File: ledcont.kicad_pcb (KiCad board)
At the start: 2 copper layers, 22 parts, among them J1 Screw_Terminal_01x02, J2 Screw_Terminal_01x02, U1 PAM2804, U2 TSM102A

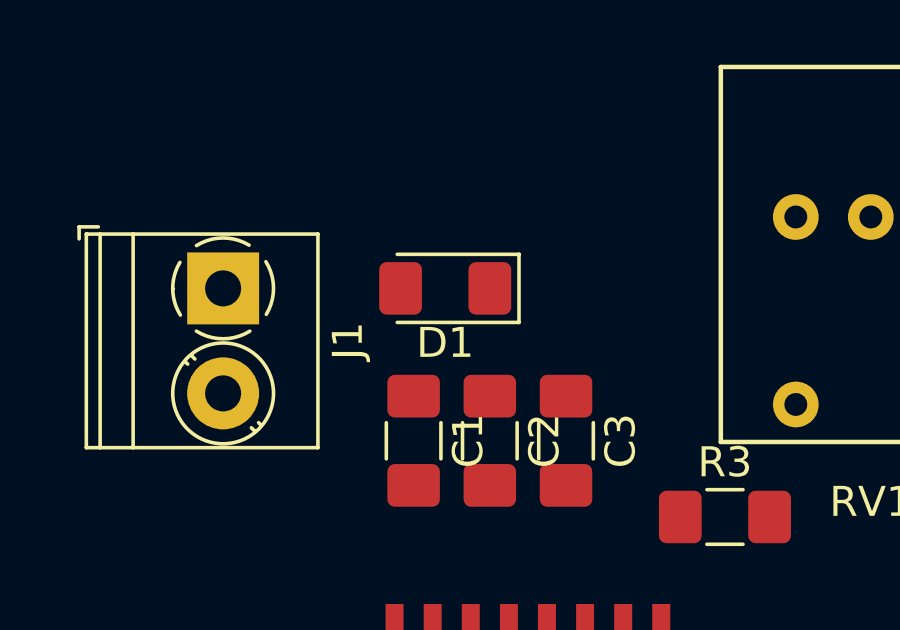
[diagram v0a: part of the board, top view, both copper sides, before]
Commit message: Updated footprints.
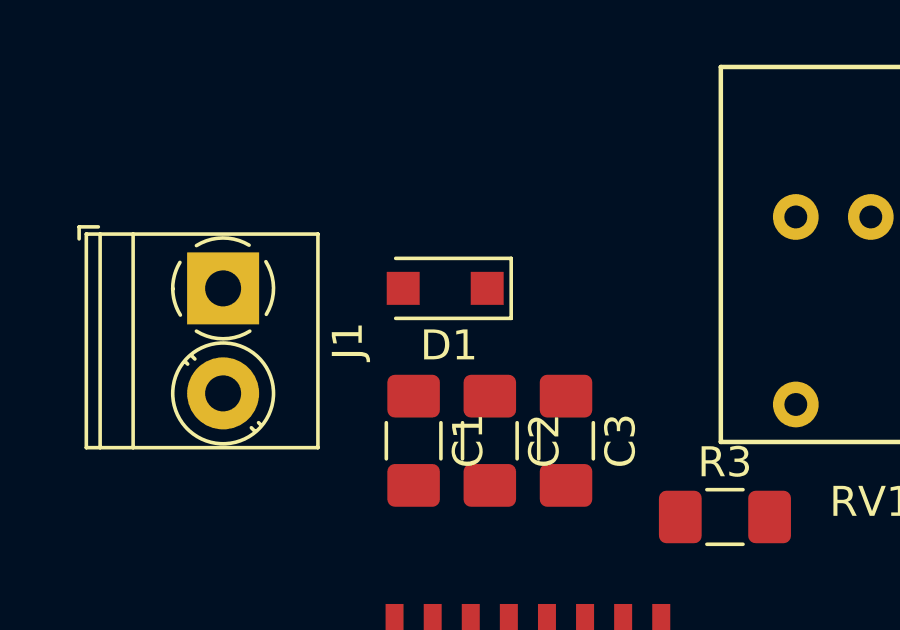
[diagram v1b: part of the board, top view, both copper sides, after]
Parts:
- D1: footprint Diode_SMD:D_1206_3216Metric_Pad1.42x1.75mm_HandSolder -> Diode_SMD:D_SOD-123F
- R9: value 0.214 -> 0.200
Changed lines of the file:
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@@
     (add_net Vref)
+  )
+  (module Diode_SMD:D_SOD-123F (layer F.Cu)
+    (at 114.0825 45.72 180)
+    (descr D_SOD-123F)
+    (tags D_SOD-123F)
+    (attr smd)
+    (fp_text reference D1 (at -0.127 -1.905 180) (layer F.SilkS)
+      (effects (font (size 1 1) (thickness 0.15)))
+    )
+    (fp_text value D_Schottky (at 0 2.1 180) (layer F.Fab)
+      (effects (font (size 1 1) (thickness 0.15)))
+    )
+    (fp_text user %R (at -0.127 -1.905 180) (layer F.Fab)
+      (effects (font (size 1 1) (thickness 0.15)))
+    )
+    (fp_line (start -2.2 -1) (end -2.2 1) (layer F.SilkS) (width 0.12))
+    (fp_line (start 0.25 0) (end 0.75 0) (layer F.Fab) (width 0.1))
+    (fp_line (start 0.25 0.4) (end -0.35 0) (layer F.Fab) (width 0.1))
+    (fp_line (start 0.25 -0.4) (end 0.25 0.4) (layer F.Fab) (width 0.1))
+    (fp_line (start -0.35 0) (end 0.25 -0.4) (layer F.Fab) (width 0.1))
+    (fp_line (start -0.35 0) (end -0.35 0.55) (layer F.Fab) (width 0.1))
+    (fp_line (start -0.35 0) (end -0.35 -0.55) (layer F.Fab) (width 0.1))
+    (fp_line (start -0.75 0) (end -0.35 0) (layer F.Fab) (width 0.1))
+    (fp_line (start -1.4 0.9) (end -1.4 -0.9) (layer F.Fab) (width 0.1))
+    (fp_line (start 1.4 0.9) (end -1.4 0.9) (layer F.Fab) (width 0.1))
+    (fp_line (start 1.4 -0.9) (end 1.4 0.9) (layer F.Fab) (width 0.1))
+    (fp_line (start -1.4 -0.9) (end 1.4 -0.9) (layer F.Fab) (width 0.1))
+    (fp_line (start -2.2 -1.15) (end 2.2 -1.15) (layer F.CrtYd) (width 0.05))
+    (fp_line (start 2.2 -1.15) (end 2.2 1.15) (layer F.CrtYd) (width 0.05))
+    (fp_line (start 2.2 1.15) (end -2.2 1.15) (layer F.CrtYd) (width 0.05))
+    (fp_line (start -2.2 -1.15) (end -2.2 1.15) (layer F.CrtYd) (width 0.05))
+    (fp_line (start -2.2 1) (end 1.65 1) (layer F.SilkS) (width 0.12))
+    (fp_line (start -2.2 -1) (end 1.65 -1) (layer F.SilkS) (width 0.12))
+    (pad 1 smd rect (at -1.4 0 180) (size 1.1 1.1) (layers F.Cu F.Paste F.Mask)
+      (net 2 "Net-(C1-Pad1)"))
+    (pad 2 smd rect (at 1.4 0 180) (size 1.1 1.1) (layers F.Cu F.Paste F.Mask)
+      (net 6 "Net-(D1-Pad2)"))
+    (model ${KISYS3DMOD}/Diode_SMD.3dshapes/D_SOD-123F.wrl
+      (at (xyz 0 0 0))
+      (scale (xyz 1 1 1))
+      (rotate (xyz 0 0 0))
+    )
   )
   (module ledcont:P091_S (layer F.Cu)
@@
       (net 1 GND))
     (model ${KISYS3DMOD}/Capacitor_SMD.3dshapes/C_1206_3216Metric.wrl
-      (at (xyz 0 0 0))
-      (scale (xyz 1 1 1))
-      (rotate (xyz 0 0 0))
-    )
-  )
-  (module Diode_SMD:D_1206_3216Metric_Pad1.42x1.75mm_HandSolder (layer F.Cu)
-    (at 114.0825 45.72 180)
-    (descr "Diode SMD 1206 (3216 Metric), square (rectangular) end terminal, IPC_7351 nominal, (Body size source: http://www.tortai-tech.com/upload/download/2011102023233369053.pdf), generated with kicad-footprint-generator")
-    (tags "diode handsolder")
-    (attr smd)
-    (fp_text reference D1 (at 0 -1.82 180) (layer F.SilkS)
-      (effects (font (size 1 1) (thickness 0.15)))
-    )
-    (fp_text value D_Schottky (at 0 1.82 180) (layer F.Fab)
-      (effects (font (size 1 1) (thickness 0.15)))
-    )
-    (fp_line (start 1.6 -0.8) (end -1.2 -0.8) (layer F.Fab) (width 0.1))
-    (fp_line (start -1.2 -0.8) (end -1.6 -0.4) (layer F.Fab) (width 0.1))
-    (fp_line (start -1.6 -0.4) (end -1.6 0.8) (layer F.Fab) (width 0.1))
-    (fp_line (start -1.6 0.8) (end 1.6 0.8) (layer F.Fab) (width 0.1))
-    (fp_line (start 1.6 0.8) (end 1.6 -0.8) (layer F.Fab) (width 0.1))
-    (fp_line (start 1.6 -1.135) (end -2.46 -1.135) (layer F.SilkS) (width 0.12))
-    (fp_line (start -2.46 -1.135) (end -2.46 1.135) (layer F.SilkS) (width 0.12))
-    (fp_line (start -2.46 1.135) (end 1.6 1.135) (layer F.SilkS) (width 0.12))
-    (fp_line (start -2.45 1.12) (end -2.45 -1.12) (layer F.CrtYd) (width 0.05))
-    (fp_line (start -2.45 -1.12) (end 2.45 -1.12) (layer F.CrtYd) (width 0.05))
-    (fp_line (start 2.45 -1.12) (end 2.45 1.12) (layer F.CrtYd) (width 0.05))
-    (fp_line (start 2.45 1.12) (end -2.45 1.12) (layer F.CrtYd) (width 0.05))
-    (fp_text user %R (at 0 0 180) (layer F.Fab)
-      (effects (font (size 0.8 0.8) (thickness 0.12)))
-    )
-    (pad 1 smd roundrect (at -1.4875 0 180) (size 1.425 1.75) (layers F.Cu F.Paste F.Mask) (roundrect_rratio 0.175439)
-      (net 2 "Net-(C1-Pad1)"))
-    (pad 2 smd roundrect (at 1.4875 0 180) (size 1.425 1.75) (layers F.Cu F.Paste F.Mask) (roundrect_rratio 0.175439)
-      (net 6 "Net-(D1-Pad2)"))
-    (model ${KISYS3DMOD}/Diode_SMD.3dshapes/D_1206_3216Metric.wrl
       (at (xyz 0 0 0))
       (scale (xyz 1 1 1))
@@
       (effects (font (size 1 1) (thickness 0.15)))
     )
-    (fp_text value 0.214 (at 0 1.82 180) (layer F.Fab)
-      (effects (font (size 1 1) (thickness 0.15)))
-    )
+    (fp_text value 0.200 (at 0 1.82 180) (layer F.Fab)
+      (effects (font (size 1 1) (thickness 0.15)))
+    )

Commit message: Checkpoint before real board layout.
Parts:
- C1, C2, C3, C4, C5, C6, R2, R5, R6, R8, R9: moved to B.Cu
- moved R8 54.3 mm to (121.3, 89.5), turned to 270 degrees
- moved R9 54.3 mm to (126.4, 93.9)
- moved J2 50.2 mm to (124.3, 90.7), turned to 0 degrees
- moved J1 45.6 mm to (114.6, 90.7), turned to 0 degrees
- moved C5 43.2 mm to (121.3, 84.6)
- moved L1 40.0 mm to (126.9, 84.6)
- moved U1 39.6 mm to (121.3, 84.6), turned to 270 degrees
- moved D1 38.8 mm to (116.3, 84.5), turned to 270 degrees
- moved C6 37.3 mm to (126.5, 84.6)
- moved C1 34.7 mm to (114.7, 85.5), turned to 180 degrees
- moved C2 32.1 mm to (114.7, 82.9), turned to 180 degrees
- moved C3 29.8 mm to (114.7, 80.4), turned to 180 degrees
- moved R4 28.8 mm to (126.5, 81.3), turned to 180 degrees
- moved R7 28.0 mm to (121.3, 81.3), turned to 180 degrees
- moved R3 24.7 mm to (114.2, 76.2), turned to 90 degrees
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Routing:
- removed copper zone on B.Cu, net GND

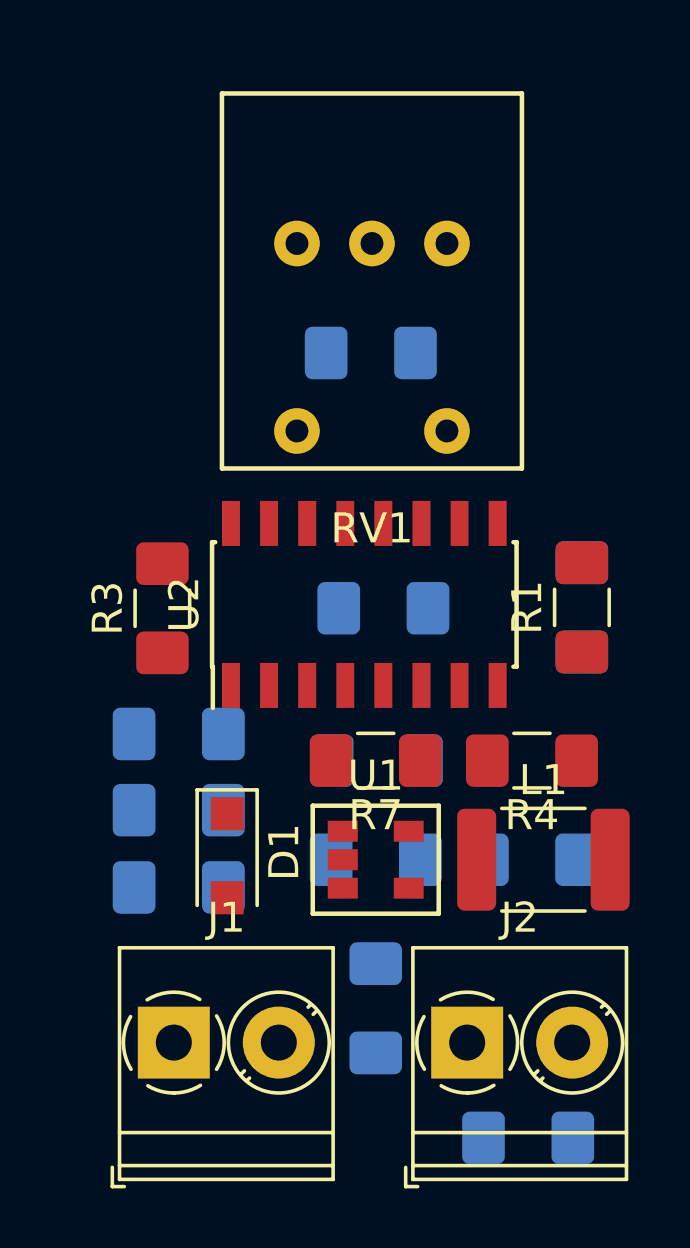
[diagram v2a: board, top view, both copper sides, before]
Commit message: Finished first attempt at board layout.
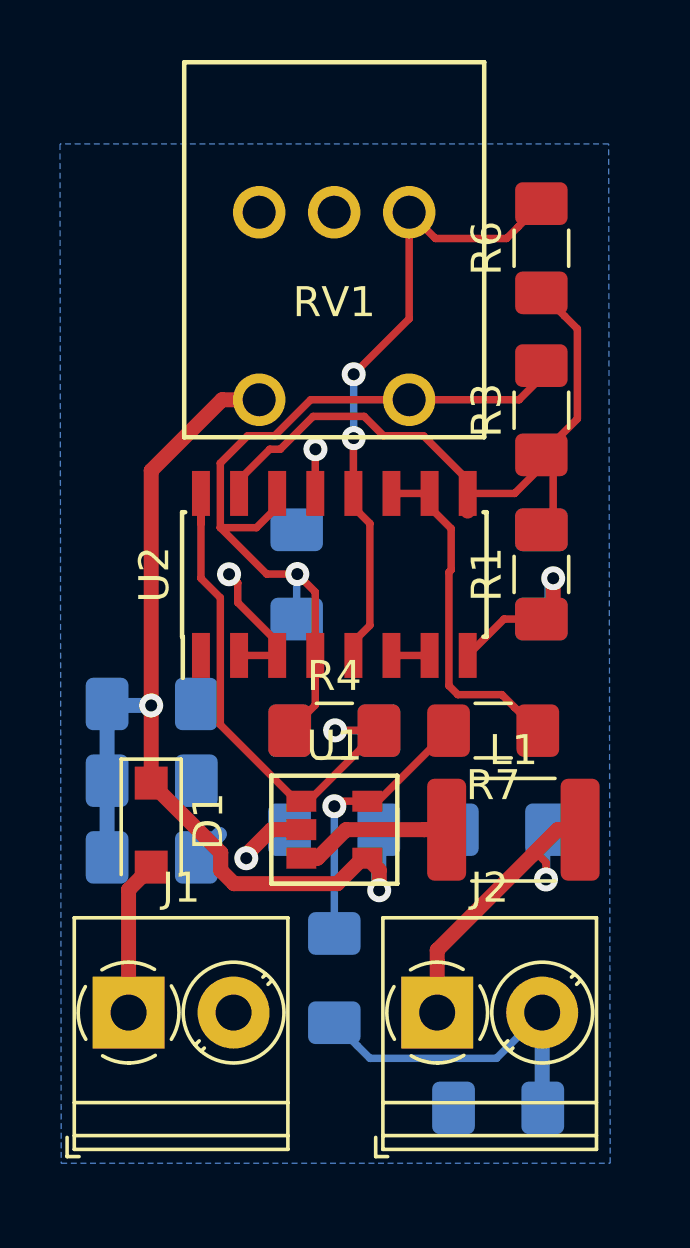
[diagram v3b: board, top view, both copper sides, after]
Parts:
- R6: moved to F.Cu
- RV1: value SPST -> 10k
- moved R3 14.3 mm to (126.8, 69.6)
- moved R6 6.67 mm to (126.8, 64.2), turned to 90 degrees
- moved R4 6.66 mm to (119.9, 80.3), turned to 0 degrees
- moved R7 4.04 mm to (125.2, 80.3)
- moved C4 3.10 mm to (118.7, 75.1), turned to 90 degrees
- moved D1 2.73 mm to (113.8, 83.4)
- moved J1 1.81 mm to (113.0, 89.7)
- moved R1 1.74 mm to (126.8, 75.1)
- moved R2 1.74 mm to (126.8, 75.1)
- moved R5 1.73 mm to (119.9, 80.3), turned to 180 degrees
- moved R8 1.71 mm to (119.9, 88.5)
- moved C5 1.71 mm to (119.9, 83.6), turned to 180 degrees
- moved U1 1.71 mm to (119.9, 83.6)
- moved RV1 1.63 mm to (119.9, 73.0)
- moved C6 1.41 mm to (125.5, 83.6)
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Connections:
- net Net-(C1-Pad1) renamed /Vin
- net Net-(R7-Pad2) renamed /Vfb
- C4 pad 1: Net-(C4-Pad1) -> /Vswitch
- R3 pad 2: Net-(C4-Pad1) -> /Vswitch
- R4 pad 1: Net-(C4-Pad1) -> /Vswitch
- R4 pad 2: Net-(R4-Pad2) -> /Ven
- R5 pad 1: Net-(R4-Pad2) -> /Ven
- RV1 pad 1: GND -> Net-(R6-Pad2)
- RV1 pad 3: Net-(R6-Pad2) -> GND
- RV1 pad 4: Net-(C4-Pad1) -> /Vswitch
- U1 pad 1: Net-(R4-Pad2) -> /Ven
- U2 pad 1: Net-(R4-Pad2) -> Net-(U2-Pad1)
- U2 pad 10: Net-(U2-Pad10) -> Net-(R7-Pad1)
- U2 pad 11: Net-(U2-Pad10) -> Net-(R7-Pad1)
- U2 pad 14: GND -> /Vswitch
- U2 pad 16: Net-(U2-Pad16) -> /Ven
- U2 pad 2: Vref -> GND
- U2 pad 3: Net-(C4-Pad1) -> GND
- U2 pad 4: Net-(C4-Pad1) -> /Vswitch
- U2 pad 6: Net-(R7-Pad1) -> Net-(U2-Pad6)
- U2 pad 7: Net-(R7-Pad1) -> Net-(U2-Pad6)
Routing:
- net /Vin: track 0.04 -> 34.2 mm, vias 0 -> 2
- net /Vswitch: track 0.00 -> 28.2 mm, vias 0 -> 1
- net Vref: track 0.00 -> 23.2 mm
- net Net-(R6-Pad2): track 0.00 -> 21.2 mm, vias 0 -> 2
- net /Ven: track 0.00 -> 19.9 mm, vias 0 -> 1
- net Net-(R7-Pad1): track 0.00 -> 11.6 mm
- net Net-(C6-Pad1): track 0.00 -> 11.3 mm, vias 0 -> 1
- net Net-(J2-Pad2): track 0.00 -> 11.2 mm
- net GND: track 0.00 -> 9.99 mm, vias 0 -> 3
- net /Vfb: track 0.00 -> 9.26 mm, vias 0 -> 1
- net Net-(R1-Pad1): track 0.00 -> 6.07 mm, vias 0 -> 1
- net Net-(L1-Pad1): track 0.00 -> 5.24 mm
- net Net-(D1-Pad2): track 0.00 -> 5.16 mm
- net Net-(U2-Pad6): track 0.00 -> 1.72 mm
- added copper zone on B.Cu, net GND

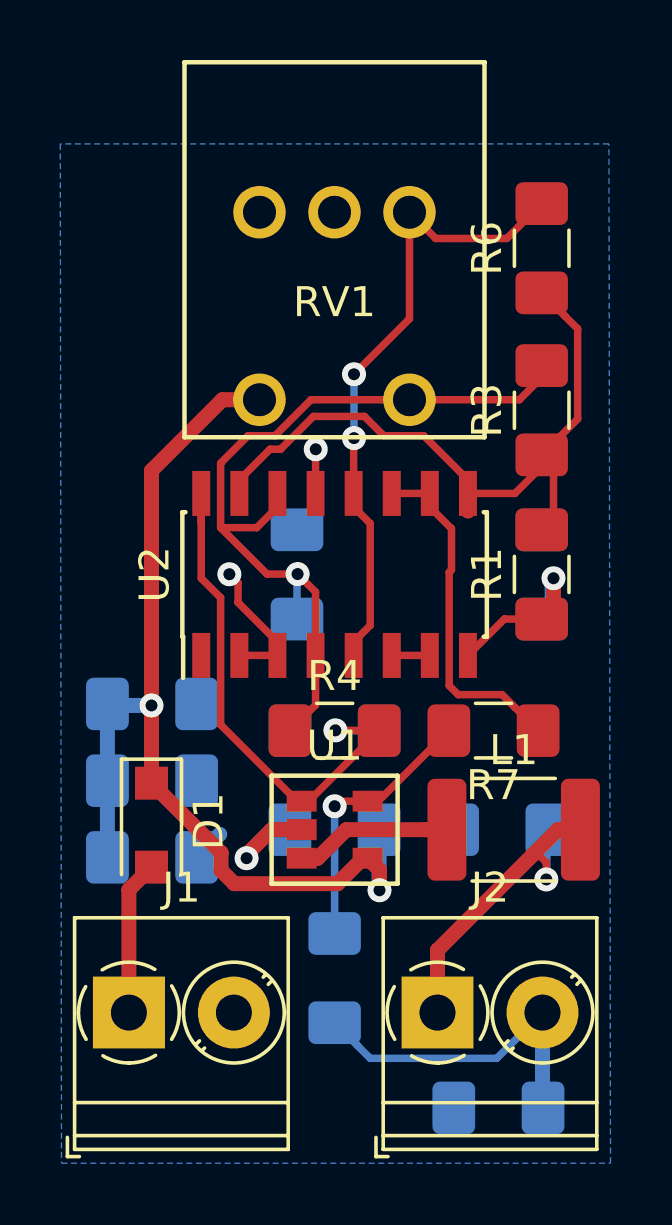
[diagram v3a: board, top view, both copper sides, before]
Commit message: Board cutout.  Rewired unused comparator.
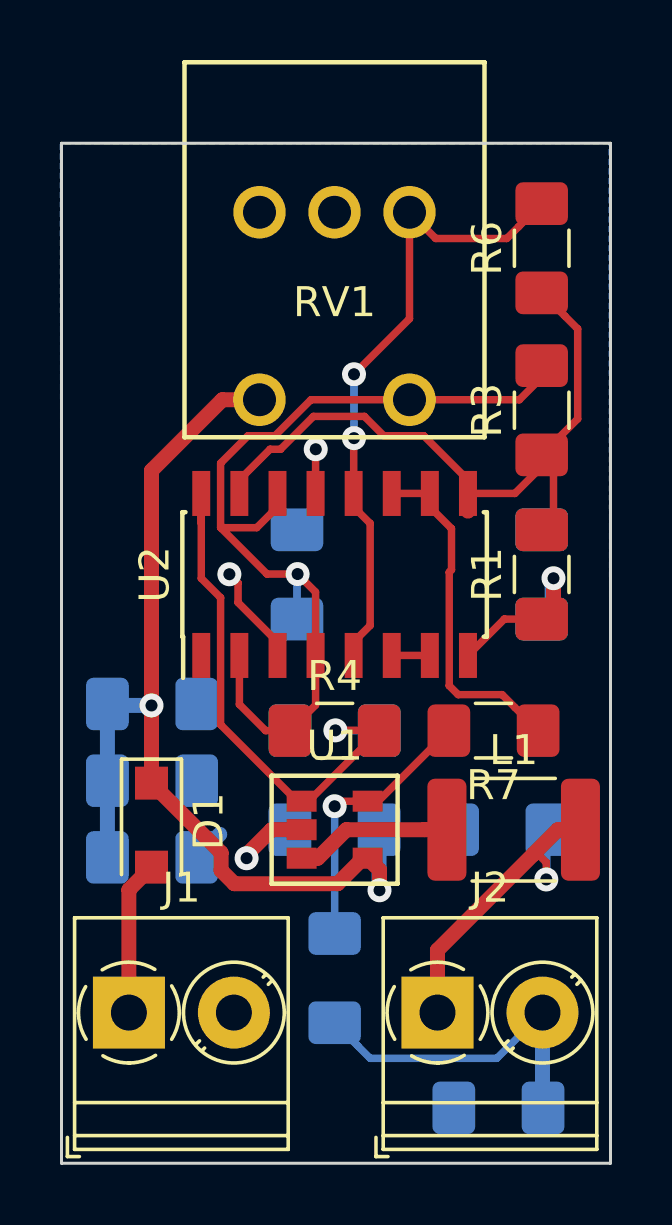
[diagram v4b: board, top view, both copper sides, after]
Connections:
- U2 pad 2: GND -> /Vswitch
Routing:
- net /Vswitch: track 28.2 -> 31.9 mm
- net GND: track 9.99 -> 8.33 mm
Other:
- board outline added: 18.3 x 34 mm
